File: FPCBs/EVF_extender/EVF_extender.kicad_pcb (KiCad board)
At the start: 2 copper layers, 82.1 x 40 mm, 2 parts, among them J3 FR02C061JA1-R5000, J4 FPC_2Rows-61Pins_0.2mm

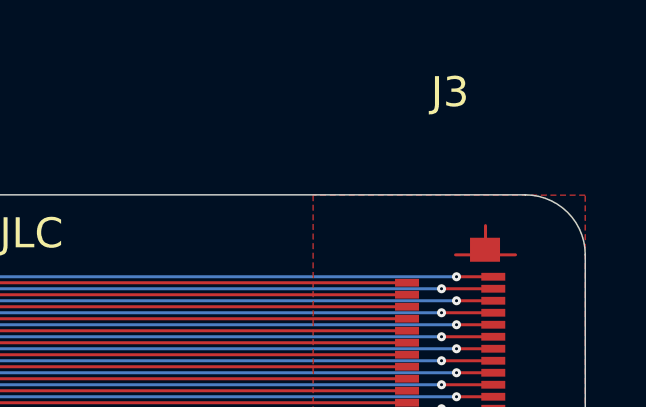
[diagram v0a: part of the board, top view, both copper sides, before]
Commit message: Add second power button
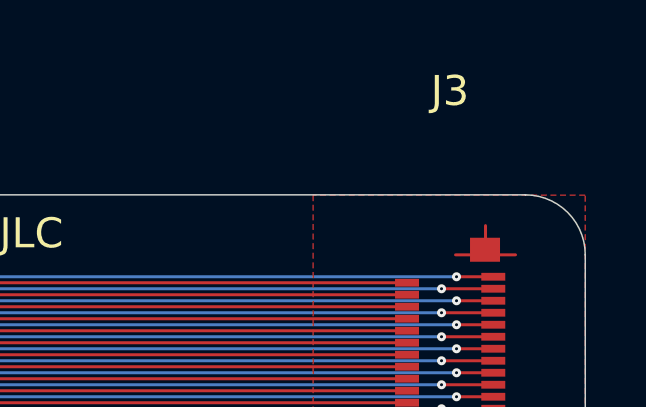
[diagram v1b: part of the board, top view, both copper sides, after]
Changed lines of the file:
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@@
 		(tags "connector Hirose  horizontal")
 		(property "Reference" "J3"
-			(at -0.035 12.15 180)
+			(at -0.03 12.19 180)
 			(layer "F.SilkS")
 			(effects
@@
 		(layer "Edge.Cuts")
 	)
+	(gr_rect
+		(start 219.51 19.05)
+		(end 235.575 21.75)
+		(stroke
+			(width 0.1)
+			(type default)
+		)
+		(fill no)
+		(layer "User.1")
+	)
+	(gr_rect
+		(start 235.575 27.08)
+		(end 251.115 47.73)
+		(stroke
+			(width 0.1)
+			(type default)
+		)
+		(fill no)
+		(layer "User.1")
+	)
+	(gr_rect
+		(start 201.335 31.25)
+		(end 235.505 43.8)
+		(stroke
+			(width 0.1)
+			(type default)
+		)
+		(fill no)
+		(layer "User.1")
+	)
 	(gr_arc

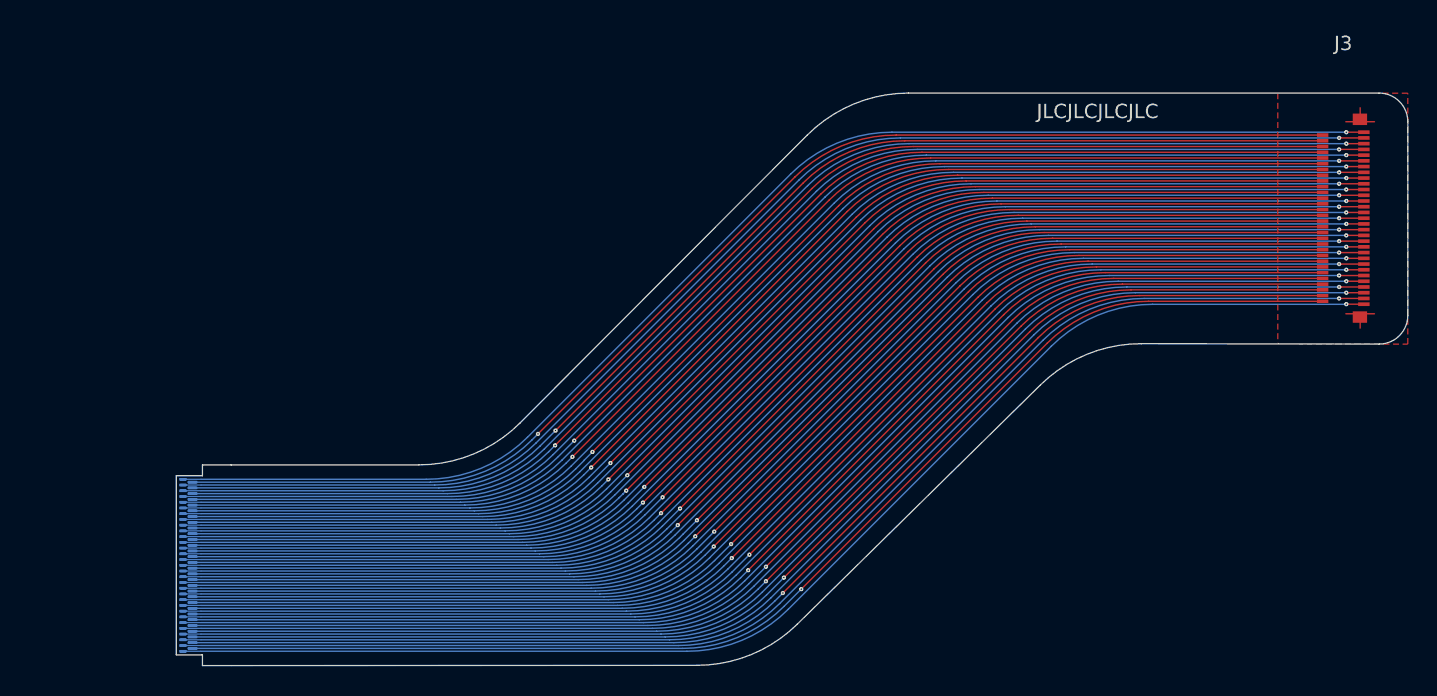
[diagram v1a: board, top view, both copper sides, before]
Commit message: Adjustments for evf and right fpcb
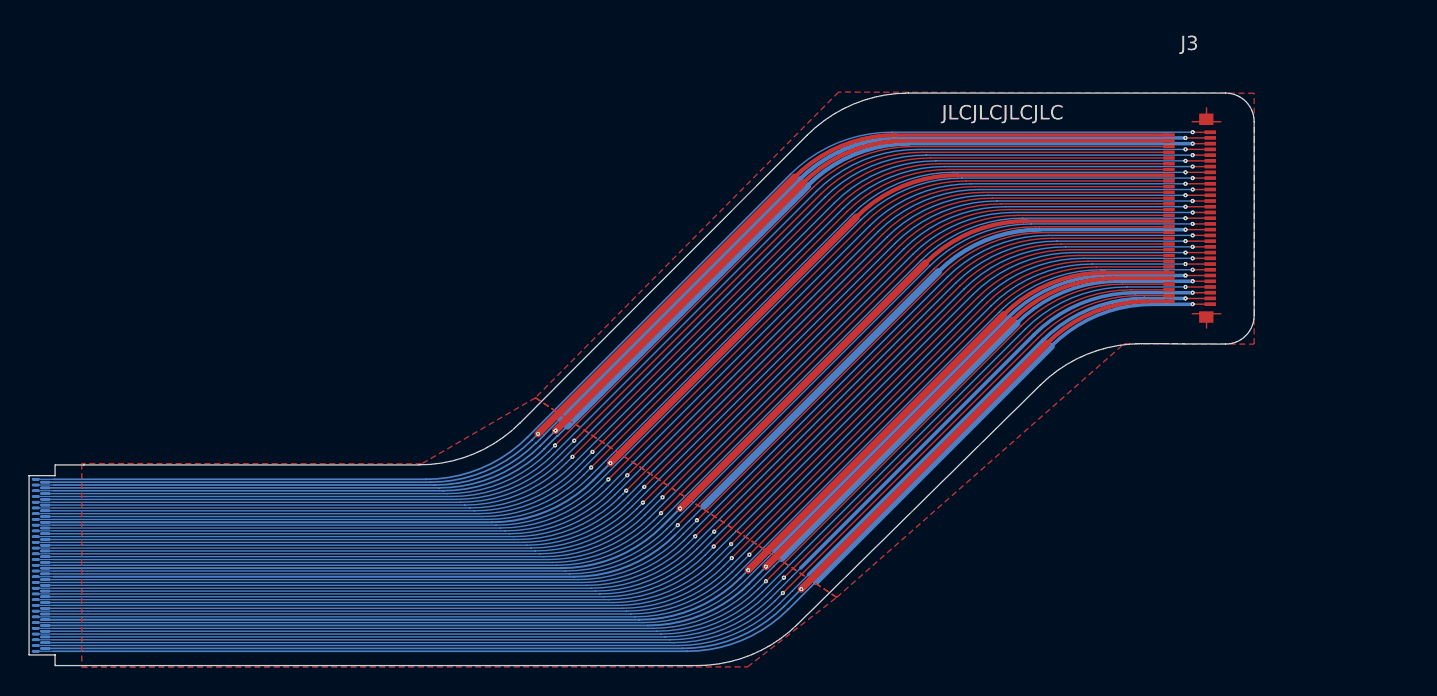
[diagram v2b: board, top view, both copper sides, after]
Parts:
- moved J3 10.7 mm to (191.0, 60.8)
- moved J4 10.3 mm to (111.9, 85.0)
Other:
- board size 82.1 x 40 mm -> 81.7 x 40 mm
